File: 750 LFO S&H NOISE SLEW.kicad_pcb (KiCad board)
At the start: 2 copper layers, 65 x 106.5 mm, 234 parts, among them J1 JACK_MONO_SW, J10 JACK_MONO_SW, J11 JACK_MONO_SW, J2 JACK_MONO_SW, J3 JACK_MONO_SW, J4 JACK_MONO_SW, J5 JACK_MONO_SW, J6 JACK_MONO_SW, J7 JACK_MONO_SW, J8 JACK_MONO_SW, J9 JACK_MONO_SW, P1 CONN_02X01, P2 CONN_02X01, P3 CONN_02X05, Q1 MMBT3904, Q10 MMBT3904, Q11 J112, Q12 MMBT3906, Q13 J112, Q14 J112, Q15 MMBT3904, Q16 MMBT3904, Q2 MMBT3904, Q3 2N7002, Q4 2N7002, Q5 MBT3946DW, Q6 DMMT3904W, Q7 MMBT3904, Q8 MMBT3904, Q9 MMBT3904, SW1 KS-01Q, SW2 KS-01Q, U1 LM13700, U10 TL072-, U11 TL072-, U12 MAX9945, U13 DG409, U14 DG409, U2 TL072-, U3 TL072-, U4 TL072-, U5 TL072-, U6 CD40106, U7 CD4027, U8 CD4027, U9 TL072-

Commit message: routing changes to pcb
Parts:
- removed C1, C2: 10μF, MyModules:2MM-POL-CAP
- removed P2: CONN_02X01, Pin_Headers:Pin_Header_Straight_1x02
- removed R109: 100, MyModules:SM0603-R-JRL
- removed R95: 2.7K, MyModules:SM0603-R-JRL
- removed TP1, TP2, TP4, TP5, TP9: CONN_1, MyModules:TEST_POINT_LOOP_4592
- added D22: 1N4148, MyModules:SOD323-JRL, B.Cu at (83.0, 55.0)
- added D23: 1N4148, MyModules:SOD323-JRL, B.Cu at (83.0, 56.8)
- added R77: 33K, MyModules:SM0603-R-JRL, B.Cu at (97.8, 108.2)
- added SW3: SPDT, MyModules:SS-12F45-1P2T-SLIDE, F.Cu at (136.0, 69.7)
- added VR9: 5K, MyModules:TC33X-2, B.Cu at (70.5, 45.0)
- C27: footprint MyModules:2MM-POL-CAP -> Capacitors_SMD:c_elec_4x5.3
- C28, C29: footprint MyModules:2MM-POL-CAP -> Capacitors_SMD:c_elec_5x5.3
- J1, J10, J11, J2, J3, J4, J6, J8, J9: value JACK_MONO_SW -> PJ301BM
- P1: value CONN_02X01 -> CONN_01X03; footprint Pin_Headers:Pin_Header_Straight_1x02 -> DIY:PAD_3
- Q6: value DMMT3904W -> MBT3946DW
- R1: value 100 -> 270K
- R2: value 100 -> 820K
- R26: value 100K -> 10K
- R4: value 390K -> 180K
- R96, R97: value 4.7K -> 2.2K
- TP7, TP8: footprint MyModules:TEST_POINT_LOOP_4592 -> MyModules:TEST_POINT_SMALL
- VR2, VR3, VR5, VR7: footprint MyModules:Bourns_3362P -> MyModules:TC33X-2
- moved P1 43.5 mm to (82.0, 48.5), turned to 180 degrees
- moved R2 33.0 mm to (81.5, 86.8), turned to 0 degrees
- moved J10 21.0 mm to (99.5, 123.5)
- moved R50 13.8 mm to (89.8, 72.0), turned to 270 degrees
- moved R9 11.0 mm to (73.8, 118.2), turned to 0 degrees
- moved VR2 10.9 mm to (78.1, 119.1)
- moved R28 10.9 mm to (92.2, 82.2)
- moved J11 10.5 mm to (117.0, 123.5)
- moved R21 10.3 mm to (92.2, 76.0), turned to 180 degrees
- moved Q10 10.2 mm to (92.2, 71.8), turned to 180 degrees
- moved R16 10.2 mm to (95.8, 79.5), turned to 90 degrees
- moved R25 10.1 mm to (89.8, 79.0), turned to 270 degrees
- moved R49 9.57 mm to (96.8, 70.5)
- moved R51 9.28 mm to (96.8, 72.2), turned to 0 degrees
- moved C44 9.00 mm to (71.5, 122.0)
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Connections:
- J11 pad 3: Net-(J10-Pad3) -> Net-(C34-Pad2)
- J2 pad 2: Net-(J2-Pad2) -> GND
- J2 pad 3: Net-(J2-Pad3) -> Net-(C18-Pad2)
- J7 pad 2: Net-(J7-Pad2) -> LFO
- J9 pad 2: S&H_INT_CLK -> Net-(J9-Pad2)
- P1 pad 1: GND -> Net-(C37-Pad2)
- P1 pad 2: Net-(J2-Pad2) -> Net-(J9-Pad2)
- Q1 pad 1: -Vn -> -12V
- Q6 pad 1: Net-(C15-Pad1) -> -12V
- Q6 pad 2: Net-(Q6-Pad2) -> Net-(C15-Pad1)
- Q6 pad 5: -12V -> Net-(Q6-Pad5)
- Q7 pad 3: +Vn -> +12V
- Q9 pad 3: +Vn -> +12V
- R1 pad 1: +Vn -> Net-(R1-Pad1)
- R10 pad 1: +Vn -> +12V
- R11 pad 2: -Vn -> -12V
- R16 pad 1: Net-(J2-Pad3) -> Net-(C18-Pad2)
- R2 pad 1: -Vn -> Net-(R2-Pad1)
- R2 pad 2: -12V -> Net-(Q5-Pad2)
- R27 pad 2: -Vn -> -12V
- R28 pad 2: Net-(Q6-Pad2) -> Net-(Q6-Pad5)
- R3 pad 1: +Vn -> +12V
- R32 pad 2: GND -> -12V
- R7 pad 2: -Vn -> -12V
- U11 pad 1: Net-(R109-Pad2) -> Net-(J10-Pad3)
- U11 pad 2: Net-(R109-Pad2) -> Net-(J10-Pad3)
- U13 pad 5: LFO_TRI -> LFO_SINE
- VR3 pad 2: Net-(Q5-Pad2) -> Net-(R2-Pad1)
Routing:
- net Net-(J9-Pad2): track 0.00 -> 96.5 mm
- net S&H_INT_CLK: track 111.8 -> 49.0 mm
- net +12V: track 580.4 -> 639.7 mm, vias 28 -> 33
- net +Vn: track 39.3 -> 0.00 mm, vias 2 -> 0
- net LFO: track 73.2 -> 111.8 mm, vias 1 -> 3
- net -Vn: track 38.3 -> 0.00 mm, vias 2 -> 0
- net -12V: track 434.7 -> 470.3 mm, vias 18 -> 25
- net GND: track 183.3 -> 148.0 mm, vias 32 -> 27
- net Net-(J2-Pad3): track 21.4 -> 0.00 mm, vias 1 -> 0
- net Net-(C37-Pad2): track 11.2 -> 26.1 mm
- net Net-(J10-Pad3): track 44.6 -> 30.2 mm
- net Net-(C18-Pad2): track 5.98 -> 20.0 mm, vias 0 -> 1
- net Net-(J8-Pad3): track 39.3 -> 29.5 mm
- net (no net): track 0.00 -> 6.19 mm
- net Net-(R14-Pad1): track 26.1 -> 20.4 mm
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
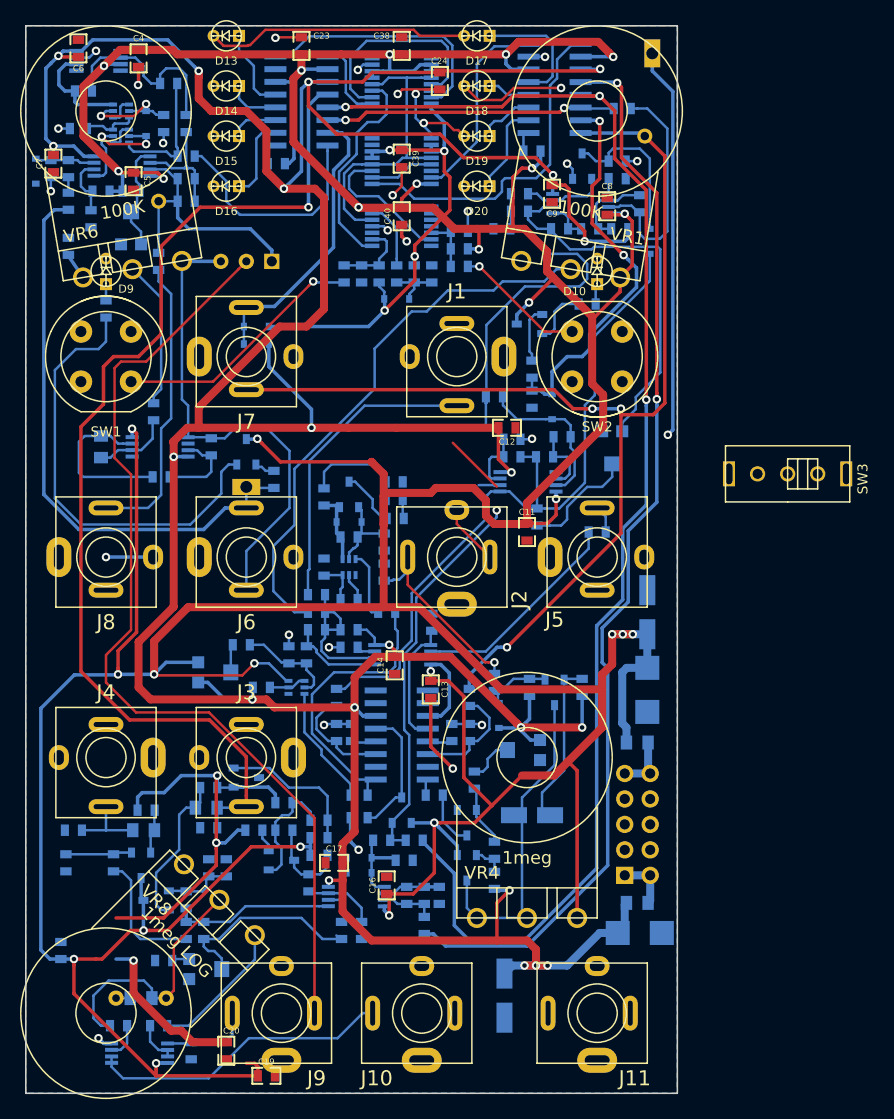
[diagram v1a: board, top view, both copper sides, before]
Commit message: almost done routing second version, 3 ground signals left to stitch
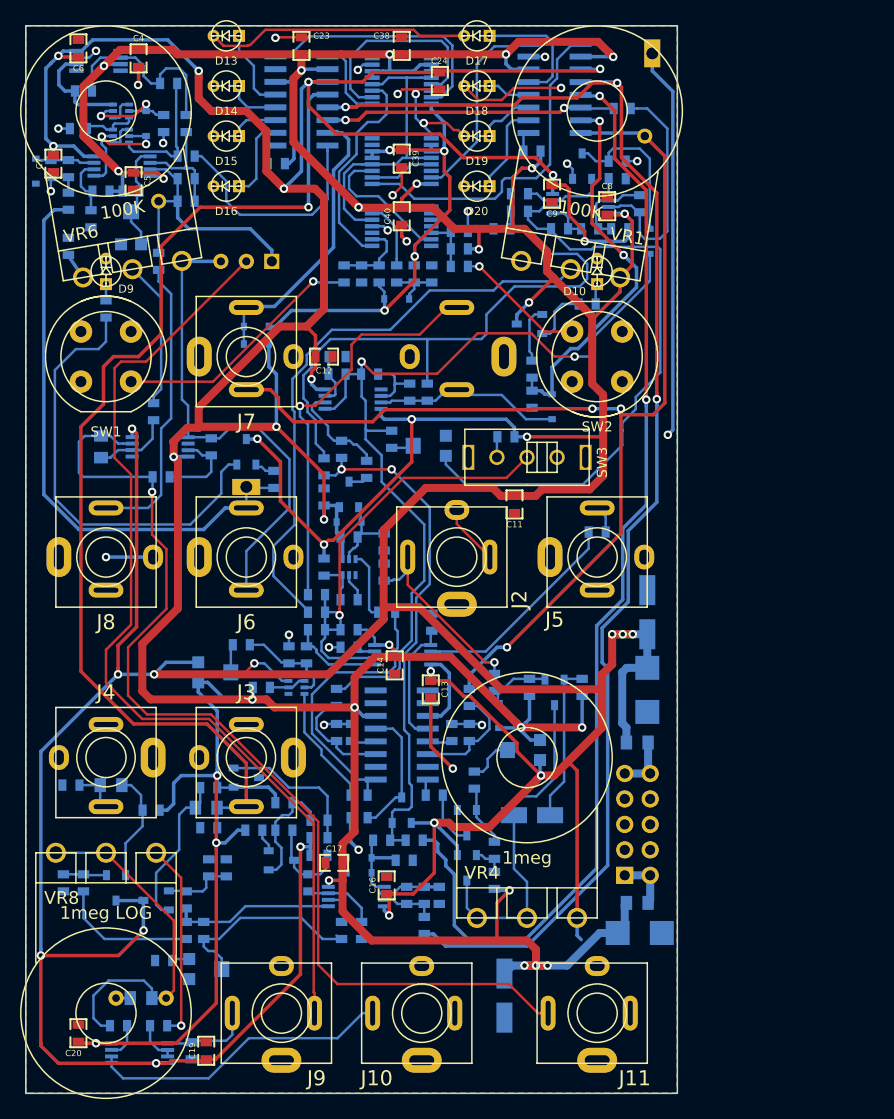
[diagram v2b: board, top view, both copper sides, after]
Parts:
- J1: moved to B.Cu
- moved R1 67.8 mm to (107.9, 66.0), turned to 0 degrees
- moved SW3 26.1 mm to (110.0, 68.0)
- moved C12 19.6 mm to (89.8, 58.0)
- moved R52 19.3 mm to (91.0, 58.0)
- moved R63 19.3 mm to (91.0, 59.8)
- moved R69 19.3 mm to (94.3, 59.8)
- moved U2 19.3 mm to (92.5, 62.2)
- moved VR7 18.4 mm to (100.1, 66.9), turned to 270 degrees
- moved R66 16.4 mm to (96.5, 66.2)
- moved R71 15.8 mm to (98.3, 61.5), turned to 270 degrees
- moved C20 14.9 mm to (65.2, 125.5), turned to 270 degrees
- moved R51 7.25 mm to (91.5, 67.2), turned to 90 degrees
- moved R49 7.16 mm to (89.8, 69.0), turned to 90 degrees
- moved R53 6.72 mm to (100.0, 61.5), turned to 90 degrees
- moved C19 6.50 mm to (78.0, 127.2), turned to 90 degrees
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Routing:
- net Net-(C34-Pad2): track 16.5 -> 103.9 mm, vias 0 -> 1
- net +12V: track 639.7 -> 672.0 mm, vias 33 -> 36
- net Net-(R13-Pad1): track 15.8 -> 45.5 mm, vias 0 -> 1
- net LFO_SINE: track 110.4 -> 137.9 mm
- net LFO_TRI: track 135.8 -> 111.3 mm
- net Net-(R49-Pad2): track 37.6 -> 61.7 mm
- net Net-(R59-Pad2): track 37.9 -> 60.3 mm
- net Net-(D7-Pad2): track 72.1 -> 89.5 mm, vias 0 -> 2
- net Net-(C44-Pad1): track 25.4 -> 36.0 mm
- net Net-(J1-Pad3): track 30.4 -> 40.3 mm, vias 0 -> 1
- net Net-(R66-Pad2): track 11.5 -> 3.15 mm
- net Net-(C31-Pad2): track 4.82 -> 11.1 mm
- net (no net): track 6.19 -> 0.01 mm
- net Net-(R36-Pad2): track 4.18 -> 10.3 mm
- net Net-(R104-Pad1): track 13.9 -> 19.7 mm, vias 0 -> 1
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
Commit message: routed
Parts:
- J1: moved to F.Cu
- moved C11 1.25 mm to (110.0, 72.8)
- moved R53 0.21 mm to (100.0, 61.8)
- moved R71 0.21 mm to (98.2, 61.8)
- turned J1 to 0 degrees
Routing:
- net GND: track 146.8 -> 162.5 mm, vias 26 -> 32
- net +12V: track 672.0 -> 661.3 mm
- net PINK_NOISE: track 105.9 -> 107.8 mm
- net Net-(R13-Pad1): track 45.5 -> 47.1 mm
- net Net-(J1-Pad3): track 40.3 -> 38.9 mm
- net LFO_PULSE: track 38.8 -> 40.0 mm
- net Net-(D7-Pad2): track 89.5 -> 88.8 mm
- net Net-(R64-Pad2): track 14.9 -> 14.2 mm
- net Net-(D8-Pad1): track 18.4 -> 17.8 mm
- net LFO: track 113.4 -> 112.9 mm

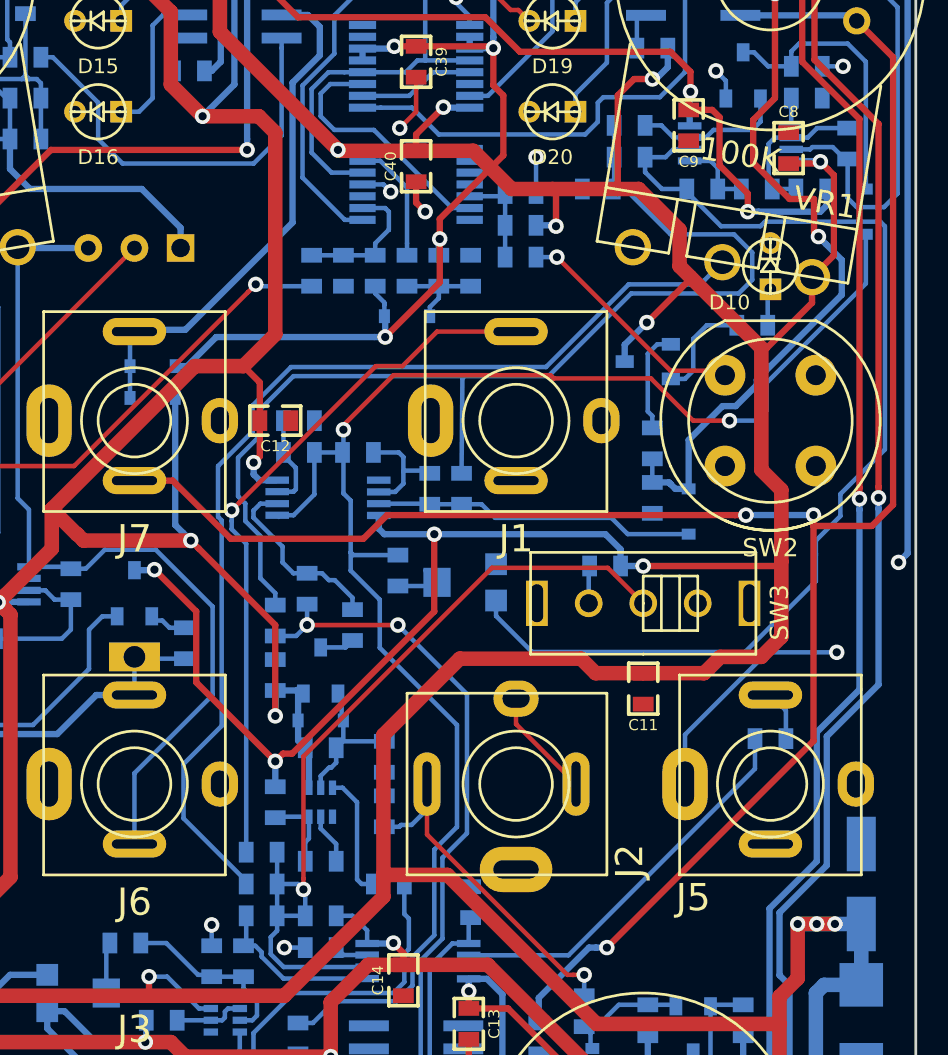
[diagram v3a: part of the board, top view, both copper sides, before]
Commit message: update test point footprint, adjust silkscreen
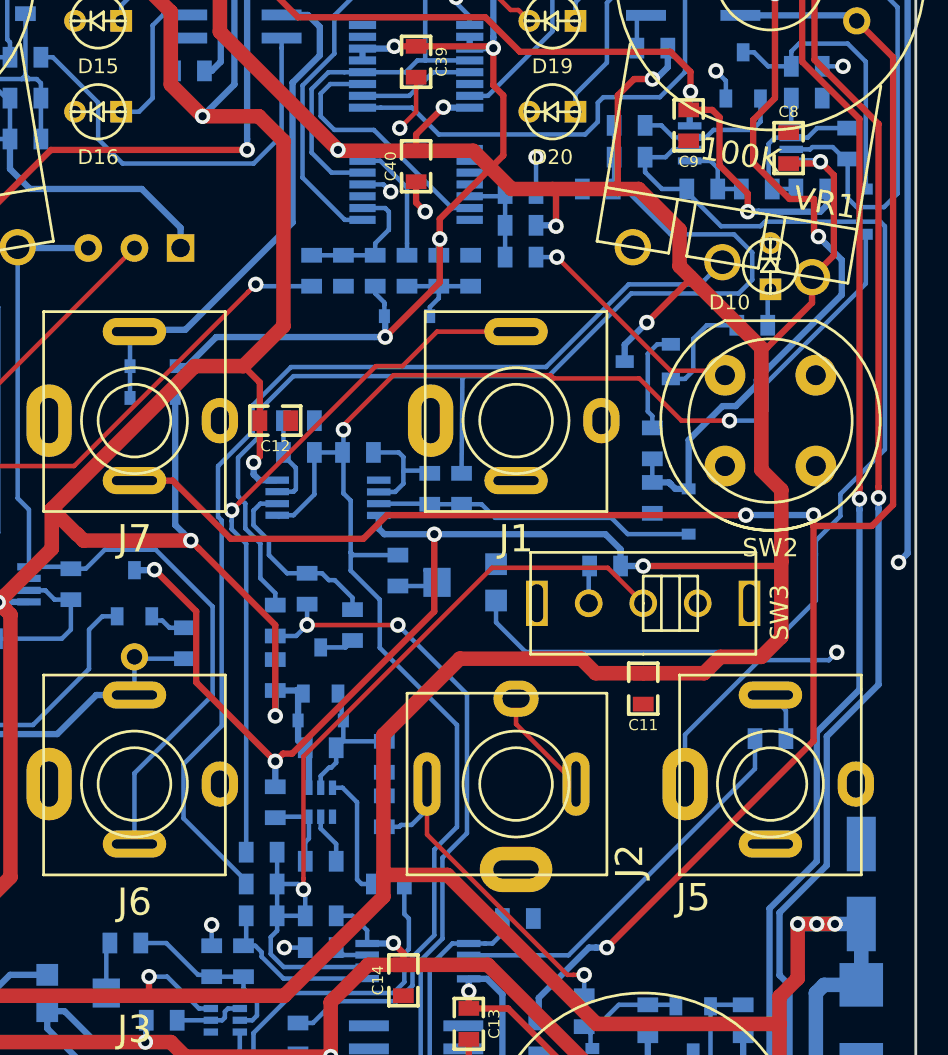
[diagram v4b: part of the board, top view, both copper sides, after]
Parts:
- TP6: footprint MyModules:TEST_POINT_LOOP_4592 -> MyModules:TEST_POINT_SMALL
- moved R58 2.75 mm to (103.1, 85.4), turned to 0 degrees
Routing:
- net Net-(R58-Pad1): track 12.7 -> 14.1 mm
- net Net-(R59-Pad2): track 60.3 -> 61.2 mm

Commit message: silkscreen tweaking. getting ready to generate gerbers and order v1.1 PCBs
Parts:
- added REF***: OSHW-Symbol_6.7x6mm_SilkScreen, Symbols:OSHW-Symbol_6.7x6mm_SilkScreen, B.Cu at (65.8, 116.0)
- P1: footprint DIY:PAD_3 -> DIY:PIN_ARRAY_3X1
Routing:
- net GND: track 162.5 -> 167.4 mm, vias 32 -> 33
- net Net-(J1-Pad3): track 38.9 -> 40.8 mm
- net +12V: track 661.3 -> 659.9 mm
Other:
- board text added: "850 LFO S&H NOISE SLEW"
- board text added: "CLK"
- board text added: "DLY LVL"
- board text added: "EXT CLOCK"
- board text added: "EXT IN"
- board text added: "FREQ CV"
- board text added: "FREQ TRIM"
- board text added: "IN"
- board text added: "LFO OUT"
- board text added: "NOISE LEVEL"
- board text added: "OUT"
- board text added: "PINK"
- board text added: "RAMP SYM"
- board text added: "RESET/GATE"
- board text added: "S&H"
- board text added: "S&H OUT"
- board text added: "SHAPE"
- board text added: "SOURCE"
- board text added: "TRI"
- board text added: "WHITE"
- board text added: "system80.net"
- board text added: "v1.1 12 2016"

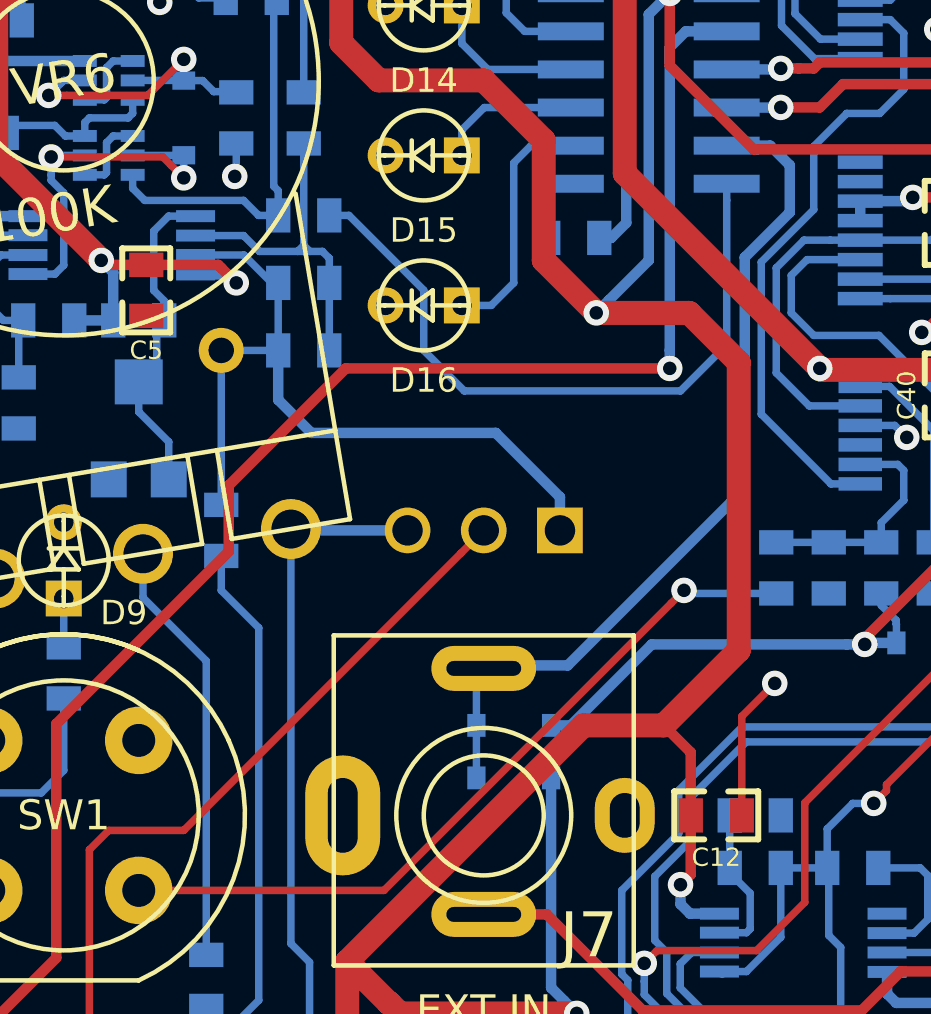
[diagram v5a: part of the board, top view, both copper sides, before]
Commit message: added buffer to s&h input
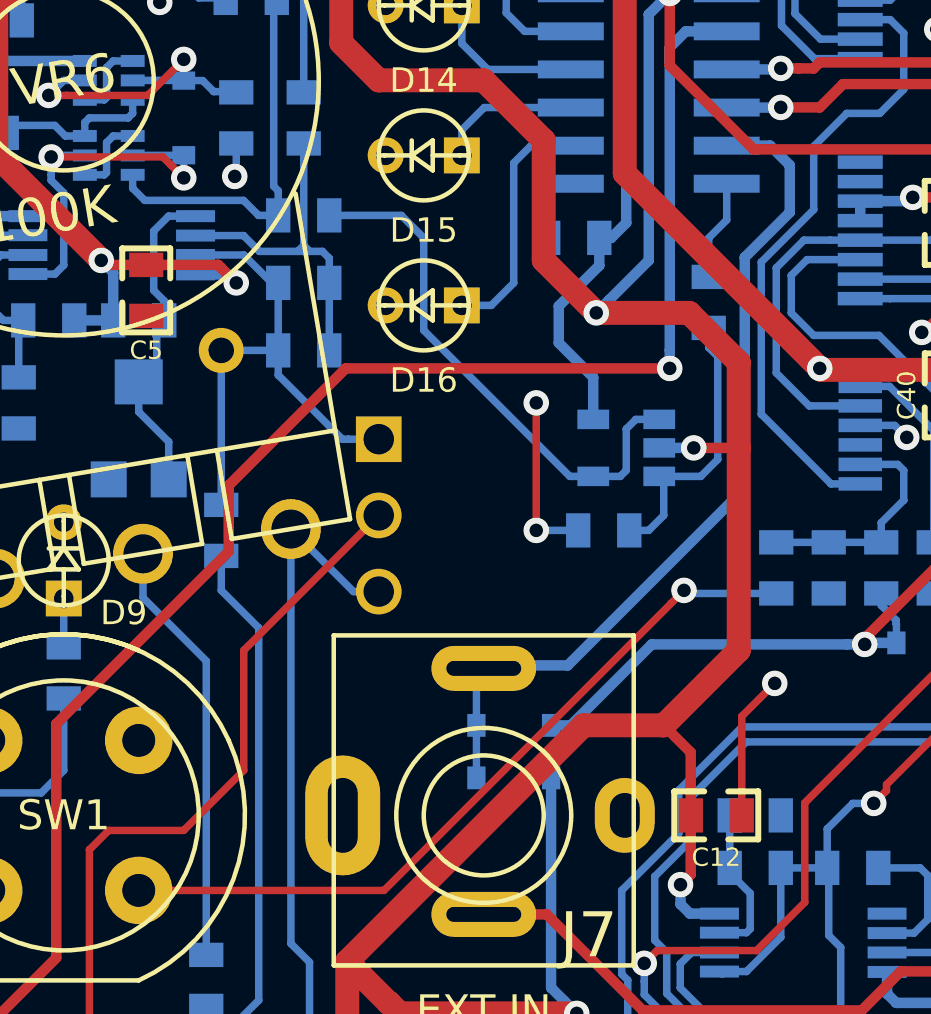
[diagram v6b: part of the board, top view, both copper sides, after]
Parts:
- added R109: 100K, MyModules:SM0603-R-JRL, B.Cu at (86.0, 48.5)
- added R95: 22K, MyModules:SM0603-R-JRL, B.Cu at (89.5, 40.9)
- added U15: TS321, TO_SOT_Packages_SMD:SOT-23-5, B.Cu at (86.8, 45.8)
- moved P1 3.54 mm to (78.5, 48.0), turned to 270 degrees
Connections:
- R89 pad 2: SAMPLE -> Net-(R89-Pad2)
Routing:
- net SAMPLE: track 22.9 -> 3.35 mm
- net Net-(R89-Pad2): track 0.00 -> 18.0 mm
- net Net-(R109-Pad2): track 0.00 -> 9.41 mm
- net Net-(C37-Pad2): track 26.1 -> 17.6 mm
- net +12V: track 659.9 -> 667.0 mm
- net GND: track 167.4 -> 173.0 mm, vias 33 -> 35
- net -12V: track 471.1 -> 473.7 mm, vias 25 -> 26
- net Net-(J9-Pad2): track 96.3 -> 95.3 mm

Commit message: ordered
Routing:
- net +12V: track 667.0 -> 664.7 mm
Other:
- rule pad_to_mask_clearance: 0.2 -> 0.01
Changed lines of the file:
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@@
     (links 497)
     (no_connects 0)
-    (area 59.924999 24.924999 125.075001 131.575001)
+    (area 51.198809 22.45604 126.9493 132.325001)
     (thickness 1.6)
     (drawings 940)
-    (tracks 1849)
+    (tracks 1847)
     (zones 0)
     (modules 233)
@@
     (pad_size 1.524 1.524)
     (pad_drill 0.762)
-    (pad_to_mask_clearance 0.2)
+    (pad_to_mask_clearance 0.01)
     (aux_axis_origin 0 0)
     (visible_elements 7FFFF77F)
@@
   (segment (start 111.3 98.25) (end 111.3 99.69) (width 0.35) (layer B.Cu) (net 4))
   (segment (start 111.3 99.69) (end 111.4 99.79) (width 0.35) (layer B.Cu) (net 4))
-  (segment (start 115 115.75) (end 115.41663 116.16663) (width 0.35) (layer B.Cu) (net 4))
-  (segment (start 115 114) (end 115 115.75) (width 0.35) (layer B.Cu) (net 4))
   (segment (start 117.6 65.75) (end 117.6 61.808996) (width 0.8) (layer F.Cu) (net 4))
   (segment (start 110 66) (end 117.35 66) (width 0.35) (layer F.Cu) (net 4))
